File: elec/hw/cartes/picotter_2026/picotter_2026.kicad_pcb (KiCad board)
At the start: 2 copper layers, 104.9 x 90.8 mm, 155 parts, among them J10 22053051, J11 22053041, J12 22053051, J13 5264-3P, J14 22053051, J15 22053051, J16 22053041, J17 22053051, J18 2-1445051-3, J19 22272031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

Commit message: pictotter: schematic fixes after review. New prelayout proposition
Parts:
- removed C38: 10µF 35V, cocotter_capacitors:C_1206_3216Metric
- removed J20: 2-1445055-3, cocotter_connectors:2-1445055-3
- added D13: DSK34, cocotter_diodes:D_SOD-123, F.Cu at (40.9, 30.3)
- added Q19: BSS84, cocotter_transistors:SOT-23-3, F.Cu at (40.6, 21.9)
- added Q20: 2N7002, cocotter_transistors:SOT-23-3, F.Cu at (40.6, 26.4)
- added R71: 100k, cocotter_resistor:r0603_reflow, F.Cu at (36.2, 20.9)
- added R72: 100k, cocotter_resistor:r0603_reflow, F.Cu at (36.2, 23.4)
- added R73: 100k, cocotter_resistor:r0603_reflow, F.Cu at (36.2, 25.9)
- added R74: 2k2 1%, cocotter_resistor:r0603_reflow, F.Cu at (36.2, 28.3)
- added R75: 10k 1%, cocotter_resistor:r0603_reflow, F.Cu at (36.2, 30.8)
- J10, J13, J14, J15, J18, J8, J9: moved to B.Cu
- J11, J16: value 22053041 -> 22272041; footprint cocotter_connectors:22053041 -> cocotter_connectors:22272041; moved to B.Cu
- J12, J17: value 22053051 -> 22272051; footprint cocotter_connectors:22053051 -> cocotter_connectors:22272051; moved to B.Cu
- J19: value 22272031 -> 2-1445051-4; footprint cocotter_connectors:22272031 -> cocotter_connectors:2-1445051-4; moved to B.Cu
- J6: value 22053041 -> 22272041; footprint cocotter_connectors:22053041 -> cocotter_connectors:22272041
- J7: value 22053051 -> 22272051; footprint cocotter_connectors:22053051 -> cocotter_connectors:22272051
- moved J15 725.3 mm to (183.6, 74.2), turned to 30 degrees
- moved J17 717.6 mm to (156.5, 83.3), turned to -105 degrees
- moved C32 710.9 mm to (185.4, 70.1), turned to -150 degrees
- moved J16 707.6 mm to (142.2, 83.7), turned to -70 degrees
- moved J14 705.2 mm to (116.4, 74.2), turned to -30 degrees
- moved C31 705.0 mm to (144.0, 79.4), turned to 120 degrees
- moved C35 702.9 mm to (162.8, 82.2), turned to 120 degrees
- moved R13 702.8 mm to (141.0, 81.3), turned to -60 degrees
- moved R14 700.7 mm to (139.7, 82.0), turned to -60 degrees
- moved R17 700.5 mm to (157.8, 81.7), turned to -60 degrees
- moved C29 699.5 mm to (127.3, 77.1), turned to 120 degrees
- moved R16 698.1 mm to (179.3, 67.1), turned to 30 degrees
- moved C34 694.6 mm to (179.4, 61.5), turned to -150 degrees
- moved R15 694.1 mm to (131.3, 80.6), turned to -150 degrees
- moved U4 691.2 mm to (182.9, 65.7), turned to -150 degrees
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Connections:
- net /outputs/CAN_H renamed /com/CAN_H
- net /outputs/CAN_L renamed /com/CAN_L
- net /outputs/can_rx_3v3 renamed /com/can_rx_3v3
- net /outputs/can_tx_3v3 renamed /com/can_tx_3v3
- C18 pad 1: /Side 0/lidar_ctrl_3v3 -> /Side 0/lidar_pwr_3v3
- C19 pad 1: /Side 0/lidar_ctrl_3v3 -> /Side 0/lidar_pwr_3v3
- C25 pad 1: /Side 0/lidar_ctrl_3v3 -> /Side 0/lidar_pwr_3v3
- C26 pad 1: /Side 0/lidar_ctrl_3v3 -> /Side 0/lidar_pwr_3v3
- C32 pad 1: /Side 0/lidar_ctrl_3v3 -> /Side 0/lidar_pwr_3v3
- C33 pad 1: /Side 0/lidar_ctrl_3v3 -> /Side 0/lidar_pwr_3v3
- J10 pad 5: /Side 0/lidar_ctrl_3v3 -> /Side 0/lidar_pwr_3v3
- J12 pad 4: /Side 0/color_led_cmd_3v3 -> /Side 120/neopixel_cmd_3v3
- J14 pad 5: /Side 0/lidar_ctrl_3v3 -> /Side 0/lidar_pwr_3v3
- J15 pad 5: /Side 0/lidar_ctrl_3v3 -> /Side 0/lidar_pwr_3v3
- J19 pad 2: /outputs/neopixel_cmd_3v3 -> GND
- J19 pad 3: +5V -> Net-(D1-A)
- J4 pad 3: /Side 0/lidar_ctrl_3v3 -> /Side 0/lidar_tx_0_3v3
- J4 pad 5: /Side 0/lidar_ctrl_3v3 -> /Side 0/lidar_pwr_3v3
- J5 pad 5: /Side 0/lidar_ctrl_3v3 -> /Side 0/lidar_pwr_3v3
- J9 pad 5: /Side 0/lidar_ctrl_3v3 -> /Side 0/lidar_pwr_3v3
- U1 pad 23: /Side 0/lidar_ctrl_3v3 -> /Side 0/lidar_tx_0_3v3
- U1 pad 33: unconnected-(U1-PC4-Pad33) -> /power/vbatt_meas_3v3
- U1 pad 34: unconnected-(U1-PC5-Pad34) -> /power/ena_vbatt_meas_3v3
- U1 pad 35: /outputs/neopixel_cmd_3v3 -> unconnected-(U1-PB0-Pad35)
- U1 pad 59: /Side 0/color_led_cmd_3v3 -> /Side 120/neopixel_cmd_3v3
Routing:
- net GND: track 0.00 -> 9.75 mm
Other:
- board size 104.9 x 90.8 mm -> 102 x 90.8 mm
- board text added: "0"
- board text added: "120"
- board text added: "240"

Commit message: picotter: layout almost done (need seriphraphy + layout cleanup)
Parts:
- removed J19: 2-1445051-4, cocotter_connectors:2-1445051-4
- added H1: MountingHole_Pad_M3, cocotter_others:MountingHole_3.2mm_M3_Pad_Via, F.Cu at (150.0, 130.0)
- added H2: MountingHole_Pad_M3, cocotter_others:MountingHole_3.2mm_M3_Pad_Via, F.Cu at (176.0, 85.0)
- added H3: MountingHole_Pad_M3, cocotter_others:MountingHole_3.2mm_M3_Pad_Via, F.Cu at (124.0, 85.0)
- added J20: 3-794630-4, cocotter_connectors:3-794630-4, B.Cu at (146.9, 114.3)
- added Q1: PJQ4465AP-AU_R2_000A1, cocotter_transistors:Diodes_PowerDI3333-8, F.Cu at (129.4, 125.8)
- moved R20 598.9 mm to (126.5, 126.0), turned to -90 degrees
- moved U1 590.5 mm to (165.5, 125.6)
- moved C8 588.2 mm to (171.3, 136.3), turned to -90 degrees
- moved C13 588.2 mm to (169.6, 136.3), turned to -90 degrees
- moved C39 584.7 mm to (142.2, 111.7), turned to -90 degrees
- moved C2 582.5 mm to (154.8, 128.1), turned to 180 degrees
- moved D1 582.0 mm to (147.0, 110.2)
- moved R2 580.4 mm to (166.1, 109.8), turned to -90 degrees
- moved C6 580.3 mm to (159.7, 136.0), turned to 180 degrees
- moved R1 578.5 mm to (182.8, 105.5), turned to 90 degrees
- moved C7 576.8 mm to (154.3, 122.2)
- moved C12 575.9 mm to (176.7, 121.5)
- moved C11 574.8 mm to (154.4, 130.3), turned to 90 degrees
- moved Y1 573.4 mm to (154.6, 125.2), turned to 90 degrees
- moved C3 572.6 mm to (154.3, 120.7), turned to 180 degrees
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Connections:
- C1 pad 1: +3V3 -> +3.3V
- C10 pad 1: +3V3 -> +3.3V
- C11 pad 1: +3V3 -> +3.3V
- C12 pad 1: +3V3 -> +3.3V
- C3 pad 1: +3V3 -> +3.3V
- C36 pad 1: +3V3 -> +3.3V
- C37 pad 1: +3V3 -> +3.3V
- C4 pad 1: +3V3 -> +3.3V
- C6 pad 1: +3V3 -> +3.3V
- C8 pad 1: +3V3 -> +3.3V
- C9 pad 1: +3V3 -> +3.3V
- J1 pad 2: +3V3 -> +3.3V
- J2 pad 1: +3V3 -> +3.3V
- R1 pad 1: +3V3 -> +3.3V
- R21 pad 2: /power/en_5v -> Net-(U6-EN)
- R22 pad 1: /power/en_5v -> Net-(U6-EN)
- R23 pad 2: /power/en_5v -> Net-(U7-EN)
- R24 pad 1: /power/en_5v -> Net-(U7-EN)
- R25 pad 2: /power/en_5v -> Net-(U8-EN)
- R26 pad 1: /power/en_5v -> Net-(U8-EN)
- U1 pad 100: +3V3 -> +3.3V
- U1 pad 11: +3V3 -> +3.3V
- U1 pad 15: /Side 0/irq_floor_3v3 -> unconnected-(U1-PC0-Pad15)
- U1 pad 17: /Side 240/irq_floor_3v3 -> /Side 0/irq_floor_3v3
- U1 pad 21: +3V3 -> +3.3V
- U1 pad 22: +3V3 -> +3.3V
- U1 pad 23: /Side 0/lidar_tx_0_3v3 -> /Side 120/lidar_tx_1_3v3
- U1 pad 24: /Side 0/lidar_rx_0_3v3 -> /Side 120/lidar_rx_1_3v3
- U1 pad 28: +3V3 -> +3.3V
- U1 pad 34: /power/ena_vbatt_meas_3v3 -> unconnected-(U1-PC5-Pad34)
- U1 pad 38: /Side 240/lidar_rx_1_3v3 -> /Side 120/lidar_rx_0_3v3
- U1 pad 39: /Side 240/lidar_tx_1_3v3 -> /Side 120/lidar_tx_0_3v3
- U1 pad 5: unconnected-(U1-PE6-Pad5) -> /power/ena_vbatt_meas_3v3
- U1 pad 50: +3V3 -> +3.3V
- U1 pad 55: /Side 120/lidar_tx_0_3v3 -> /Side 0/lidar_rx_0_3v3
- U1 pad 56: /Side 120/lidar_rx_1_3v3 -> /Side 0/lidar_tx_0_3v3
- U1 pad 6: +3V3 -> +3.3V
- U1 pad 61: /Side 120/lidar_rx_0_3v3 -> /Side 240/lidar_tx_1_3v3
- U1 pad 62: /Side 120/lidar_tx_1_3v3 -> /Side 240/lidar_rx_1_3v3
- U1 pad 68: /uc/UART_RX_PRG -> /uc/UART_TX_PRG
- U1 pad 73: +3V3 -> +3.3V
- U1 pad 75: +3V3 -> +3.3V
- U1 pad 80: unconnected-(U1-PC12-Pad80) -> /Side 240/irq_floor_3v3
- U5 pad 3: +3V3 -> +3.3V
- U6 pad 3: /power/en_5v -> Net-(U6-EN)
- U7 pad 3: /power/en_5v -> Net-(U7-EN)
- U8 pad 3: /power/en_5v -> Net-(U8-EN)
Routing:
- net +3.3V: track 0.00 -> 468.7 mm, vias 0 -> 22
- net GND: track 9.75 -> 324.3 mm, vias 0 -> 40
- net /Side 0/lidar_ctrl_3v3: track 0.00 -> 222.5 mm
- net /Side 0/lidar_pwr_3v3: track 0.00 -> 218.3 mm, vias 0 -> 3
- net /Side 0/digital_servo_cmd_g_3v3: track 0.00 -> 176.7 mm, vias 0 -> 4
- net +BATT: track 0.00 -> 157.3 mm, vias 0 -> 11
- net /Side 120/scl_3v3: track 0.00 -> 137.9 mm, vias 0 -> 2
- net /Side 120/sda_3v3: track 0.00 -> 137.6 mm, vias 0 -> 2
- net +6V: track 0.00 -> 135.2 mm
- net /Side 240/scl_3v3: track 0.00 -> 111.1 mm, vias 0 -> 6
- net /Side 240/sda_3v3: track 0.00 -> 107.3 mm, vias 0 -> 5
- net +5V: track 0.00 -> 104.9 mm, vias 0 -> 3
- net /Side 120/lidar_rx_0_3v3: track 0.00 -> 96.7 mm, vias 0 -> 2
- net /Side 120/lidar_tx_0_3v3: track 0.00 -> 94.7 mm, vias 0 -> 2
- net /Side 240/lidar_tx_0_3v3: track 0.00 -> 92.7 mm, vias 0 -> 2
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- added copper zone on F.Cu, net +3.3V
- added copper zone on In1.Cu, net GND
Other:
- board size 102 x 90.8 mm -> 100.5 x 87 mm
- copper layers 2 -> 4

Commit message: picotter: final layout
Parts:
- moved C16 0.40 mm to (168.9, 140.4)
- moved C44 0.14 mm to (113.3, 105.2)
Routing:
- net /Side 240/irq_floor_3v3: track 64.0 -> 61.8 mm
- net +BATT: track 157.3 -> 155.3 mm
- net /Side 240/lidar_rx_0_3v3: track 86.6 -> 88.4 mm
- net unconnected-(U1-PC0-Pad15): track 1.82 -> 0.00 mm
- net /Side 240/scl_3v3: track 111.1 -> 110.0 mm
- net /Side 240/lidar_tx_0_3v3: track 92.7 -> 93.8 mm
- net /Side 0/lidar_tx_0_3v3: track 59.4 -> 58.4 mm
- net +3.3V: track 468.7 -> 467.8 mm, vias 22 -> 20
- net /Side 120/lidar_tx_0_3v3: track 94.7 -> 95.4 mm
- net /Side 120/lidar_rx_0_3v3: track 96.7 -> 97.5 mm
- net /Side 120/scl_3v3: track 137.9 -> 138.6 mm
- net /Side 120/sda_3v3: track 137.6 -> 138.3 mm
- net /Side 120/irq_floor_3v3: track 79.4 -> 80.1 mm
- net /Side 0/lidar_ctrl_3v3: track 222.5 -> 223.2 mm
- added copper zone on In2.Cu, net +3.3V
- added copper zone on In2.Cu, net +5V
- added copper zone on F.Cu, net +BATT
- added copper zone on In2.Cu, net +BATT
- added copper zone on In2.Cu, net /Side 0/lidar_pwr_3v3
- added copper zone on B.Cu, net GND
- added copper zone on F.Cu, net GND
- added copper zone on In2.Cu, net GND
- added copper zone on F.Cu, net Net-(D1-A)
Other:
- board text added: "+"
- board text added: "-"
- board text added: "Cocotter Picotter 2026"
- board text removed: "0"
- board text removed: "120"
- board text removed: "240"

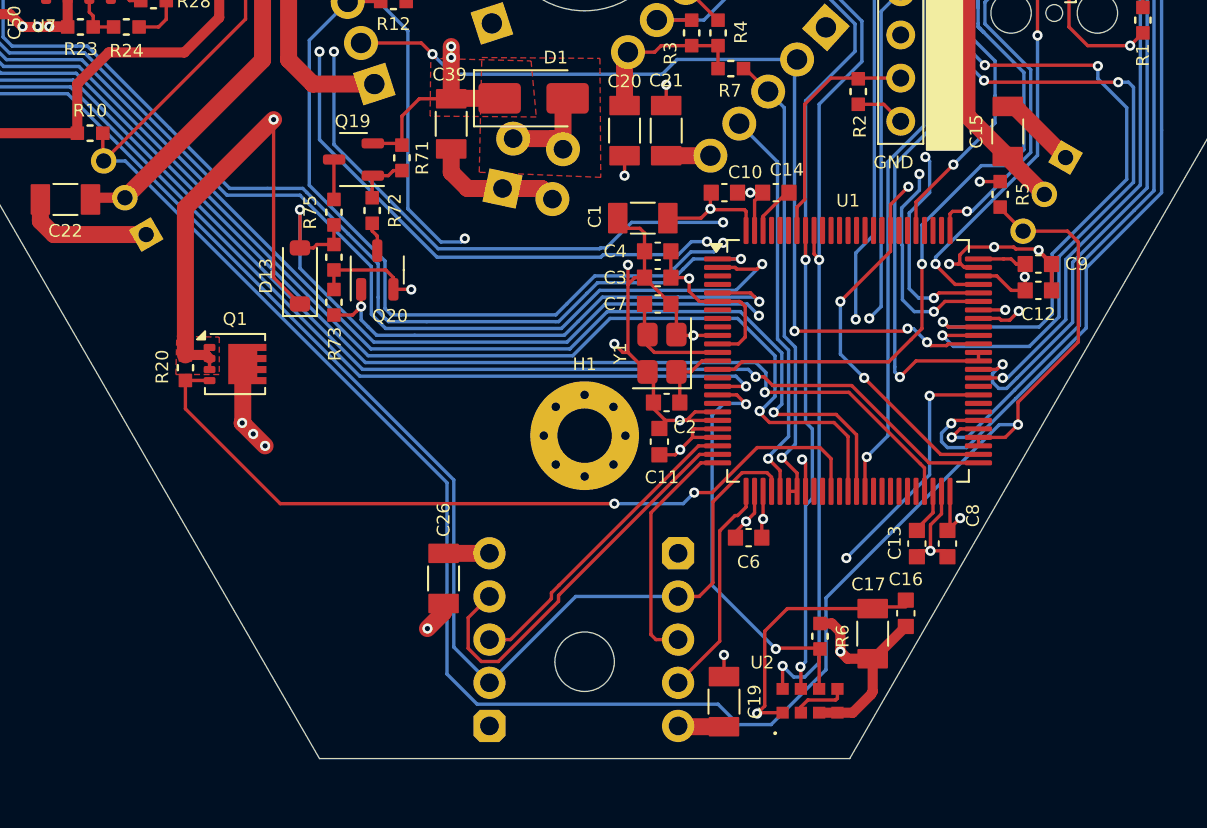
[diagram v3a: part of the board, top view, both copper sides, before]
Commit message: picotter: add led + 8 testpoints
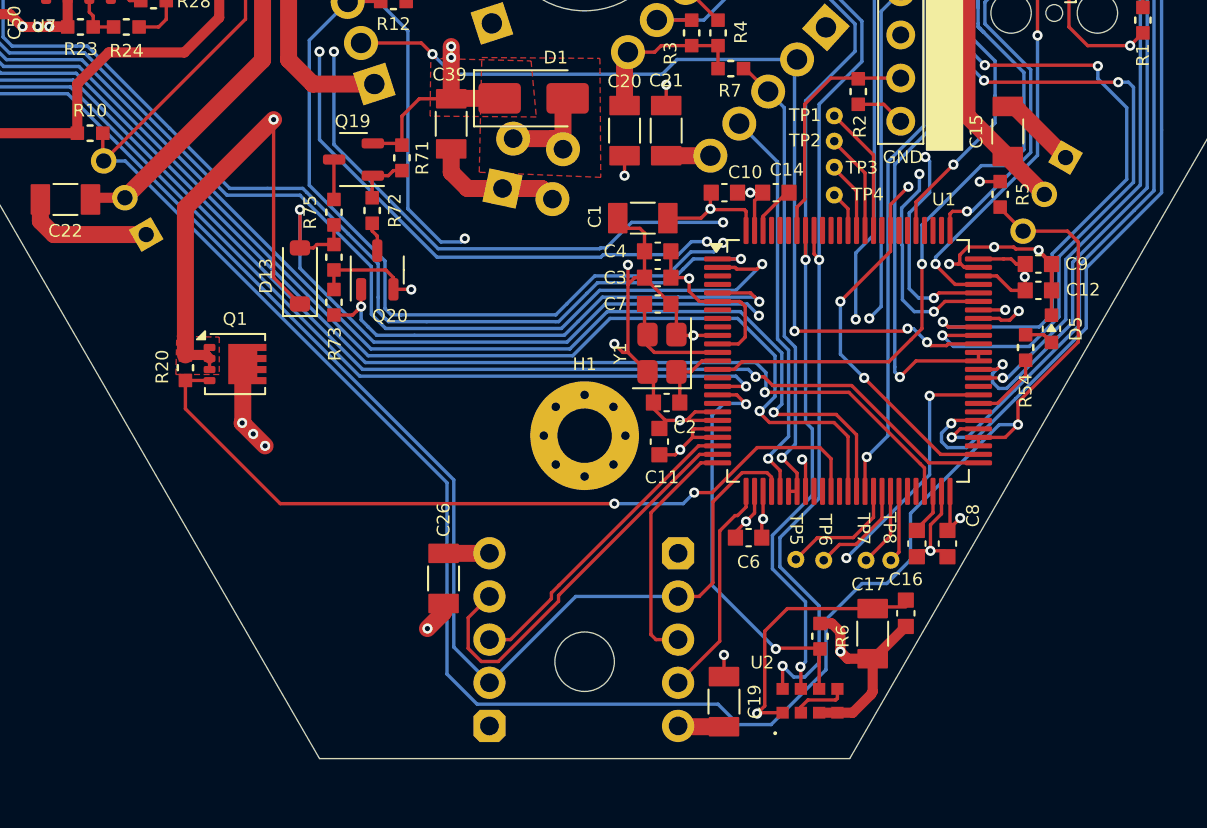
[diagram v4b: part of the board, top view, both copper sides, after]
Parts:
- added D5: green, 0603, cocotter_diodes:LED_0603_1608Metric, F.Cu at (177.5, 123.7)
- added R54: 1k 1%, cocotter_resistor:r0603_reflow, F.Cu at (175.9, 124.8)
- added TP1: TestPoint, cocotter_others:testpoint-THT-0.5mm, F.Cu at (164.7, 111.2)
- added TP2: TestPoint, cocotter_others:testpoint-THT-0.5mm, F.Cu at (164.7, 112.7)
- added TP3: TestPoint, cocotter_others:testpoint-THT-0.5mm, F.Cu at (164.7, 114.2)
- added TP4: TestPoint, cocotter_others:testpoint-THT-0.5mm, F.Cu at (164.7, 115.8)
- added TP5: TestPoint, cocotter_others:testpoint-THT-0.5mm, F.Cu at (162.4, 137.3)
- added TP6: TestPoint, cocotter_others:testpoint-THT-0.5mm, F.Cu at (164.1, 137.3)
- added TP7: TestPoint, cocotter_others:testpoint-THT-0.5mm, F.Cu at (166.6, 137.3)
- added TP8: TestPoint, cocotter_others:testpoint-THT-0.5mm, F.Cu at (168.0, 137.3)
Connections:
- U1 pad 41: unconnected-(U1-PE10-Pad41) -> Net-(U1-PE10)
- U1 pad 42: unconnected-(U1-PE11-Pad42) -> Net-(U1-PE11)
- U1 pad 43: unconnected-(U1-PE12-Pad43) -> Net-(U1-PE12)
- U1 pad 44: unconnected-(U1-PE13-Pad44) -> Net-(U1-PE13)
- U1 pad 58: unconnected-(U1-PD11-Pad58) -> /uc/led
- U1 pad 85: unconnected-(U1-PD4-Pad85) -> Net-(U1-PD4)
- U1 pad 86: unconnected-(U1-PD5-Pad86) -> Net-(U1-PD5)
- U1 pad 87: unconnected-(U1-PD6-Pad87) -> Net-(U1-PD6)
- U1 pad 88: unconnected-(U1-PD7-Pad88) -> Net-(U1-PD7)
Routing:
- net Net-(U1-PD4): track 0.00 -> 7.70 mm
- net Net-(U1-PE10): track 0.00 -> 7.13 mm
- net Net-(U1-PE11): track 0.00 -> 6.04 mm
- net Net-(U1-PD5): track 0.00 -> 5.94 mm
- net Net-(U1-PE12): track 0.00 -> 4.65 mm
- net /uc/led: track 0.00 -> 4.35 mm
- net Net-(U1-PE13): track 0.00 -> 4.25 mm
- net Net-(U1-PD6): track 0.00 -> 4.18 mm
- net Net-(U1-PD7): track 0.00 -> 2.42 mm
- net /Side 0/scl_3v3: track 58.6 -> 60.5 mm
- net Net-(D5-PadA): track 0.00 -> 1.71 mm
- net +3.3V: track 467.8 -> 469.5 mm
- net /Side 0/sda_3v3: track 58.5 -> 60.1 mm
- net GND: track 324.3 -> 325.8 mm
- net /Side 0/digital_servo_cmd_g_3v3: track 176.7 -> 177.6 mm

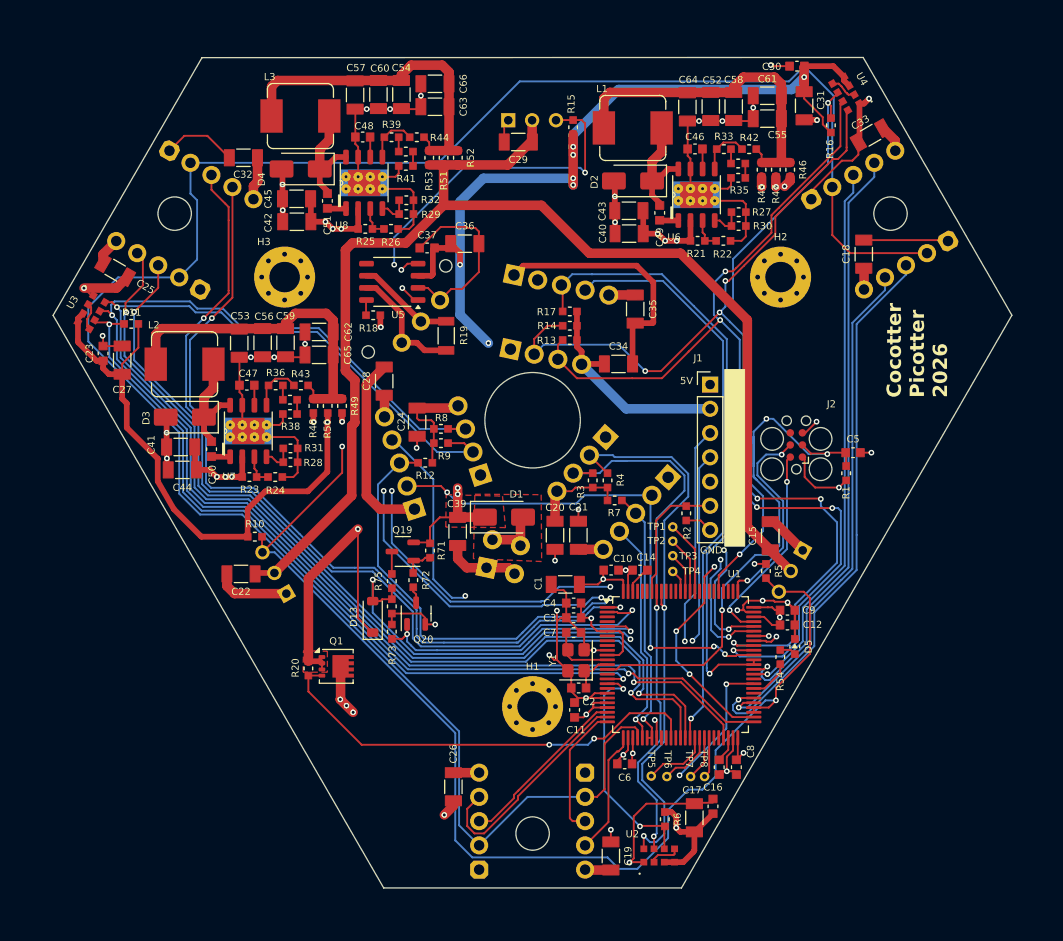
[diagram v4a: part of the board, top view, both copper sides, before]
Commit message: picotter : routing review and silkscreen modified
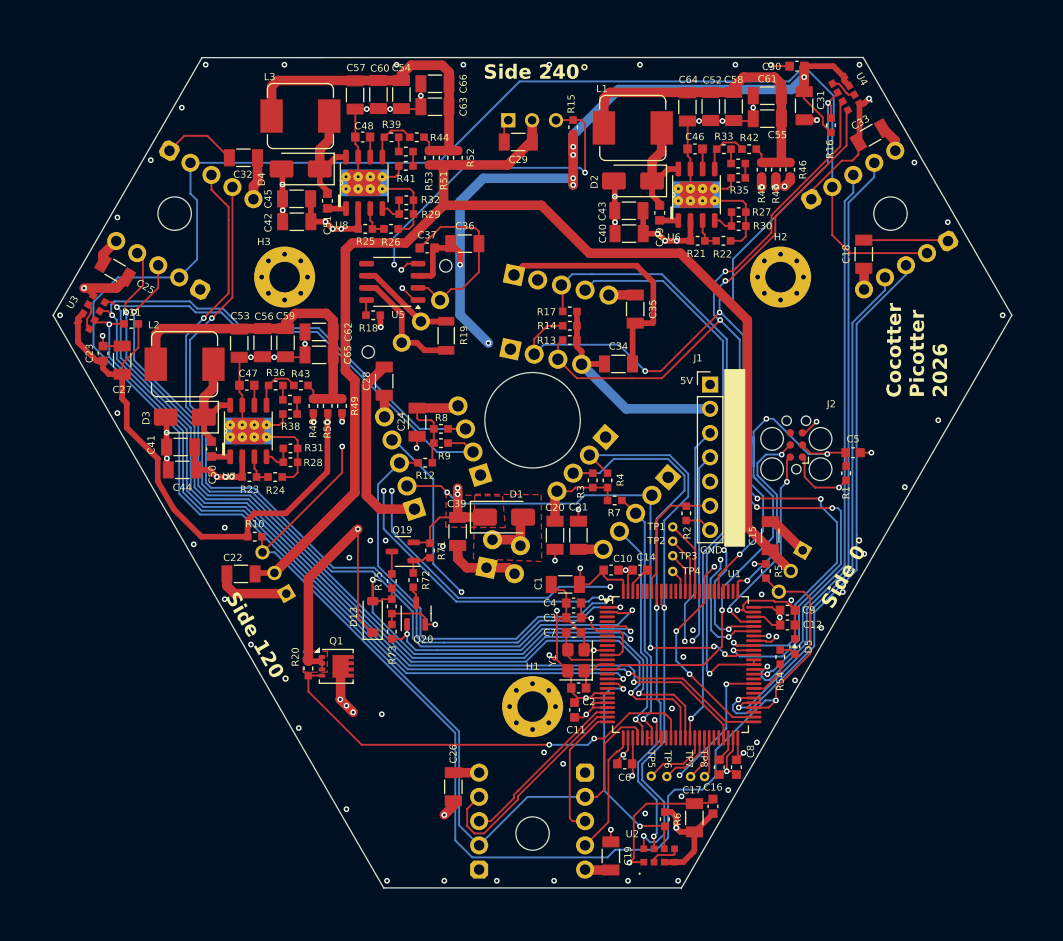
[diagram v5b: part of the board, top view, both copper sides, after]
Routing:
- net +3.3V: track 469.5 -> 474.4 mm
- net /uc/RST_PRG: track 69.5 -> 68.0 mm
- net /com/can_rx_3v3: track 87.0 -> 85.6 mm
- net /Side 120/neopixel_cmd_3v3: track 73.5 -> 72.4 mm
- net /com/can_tx_3v3: track 84.6 -> 83.5 mm
- net /Side 0/sda_3v3: track 60.1 -> 59.2 mm
- net /uc/SWCLK_PRG: track 21.5 -> 20.8 mm
- net GND: vias 40 -> 88
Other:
- board text added: "Side 0°"
- board text added: "Side 120°"
- board text added: "Side 240°"
